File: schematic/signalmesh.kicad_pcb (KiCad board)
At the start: 2 copper layers, 387 x 151 mm, 136 parts, among them J1 FPGA I/O, J10 INA219_CONFIG, J11 INA219_CONFIG, J12 AAM_DBG, J13 DSM_DBG, J14 ACM_DBG, J15 INA219_CONFIG, J16 DSM_DBG, J17 LCD_display, J18 LCD_display, J2 FPGA I/O, J3 LCD_display, J4 TDM_DBG, J5 INA219_CONFIG, J6 INA219_CONFIG, J7 INA219_CONFIG, J8 FPGA I/O, J9 FPGA I/O, U1 NUCLEO-H753ZI, U10 INA219AxD, U11 INA219AxD, U12 INA219AxD, U13 INA219AxD, U14 W25Q128JVS, U15 AP2112K-3.3, U16 74HC4050D, U17 NUCLEO-H753ZI, U18 HDSP-7503, U19 HDSP-7503, U2 HDSP-7503, U20 INA219AxD, U21 74HC4050D, U22 AP2112K-3.3, U23 W25Q128JVS, U24 74HC4050D, U25 AP2112K-3.3, U26 W25Q128JVS, U27 MCP2551-I-P, U28 74LVC1G3157, U29 MCP2551-I-P, U3 NUCLEO-F303RE, U30 MCP2551-I-P, U31 MCP2551-I-P, U4 YAAJ_BluePill_Part_Like, U5 24LC256-I_SN, U6 BME280, U7 INA219AxD, U8 24LC256-I_SN, U9 NUCLEO-F446RE

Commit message: all connections appear valid. some silkscreen clipping
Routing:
- net GND: track 169.3 -> 142.3 mm
- net ACM_SPI_MOSI: track 129.6 -> 107.5 mm
- net /CAN-: track 84.8 -> 64.5 mm, vias 0 -> 2
- net TDM_VDD: track 324.2 -> 314.5 mm, vias 4 -> 5
- net UUM_SPI1_MISO: track 66.4 -> 75.1 mm, vias 1 -> 2
- net Net-(U14-DO/IO_{1}): track 20.6 -> 28.7 mm, vias 0 -> 2
- net 5V_7SDD: track 457.5 -> 465.5 mm
- net AAM_FMC_D10: track 88.8 -> 80.9 mm, vias 1 -> 2
- net Net-(D26-A): track 11.6 -> 3.88 mm
- net TDM_I2C1_SCL: track 360.0 -> 352.6 mm, vias 6 -> 8
- net AAM_FMC_D11: track 79.4 -> 72.4 mm
- net AAM_FMC_D8: track 90.3 -> 83.4 mm
- net DSM_DBG_RX: track 87.4 -> 94.1 mm, vias 0 -> 1
- net DSM_VDD: track 182.4 -> 175.7 mm
- net UUM_SPI1_MISO_B: track 33.3 -> 26.8 mm
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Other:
- copper layers 2 -> 4

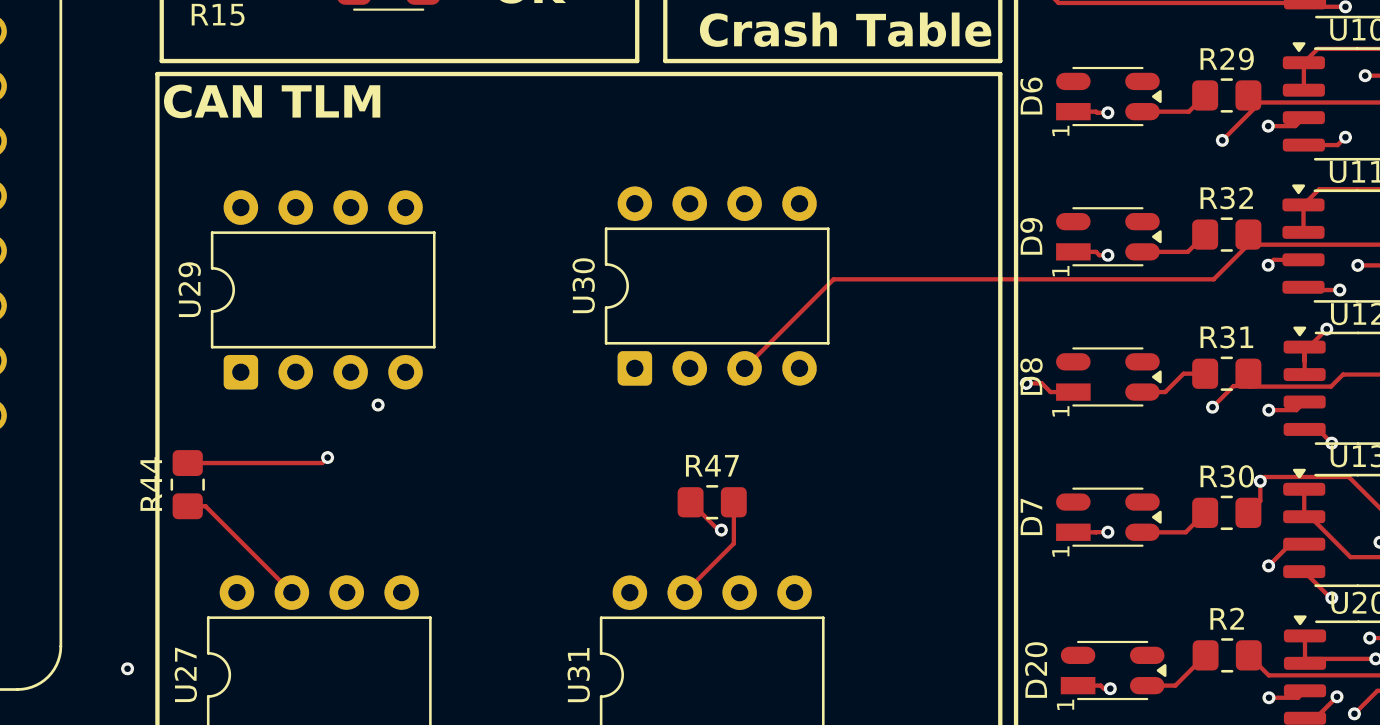
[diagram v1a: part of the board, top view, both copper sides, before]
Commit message: my CAN trscvr LAYOUT sucks
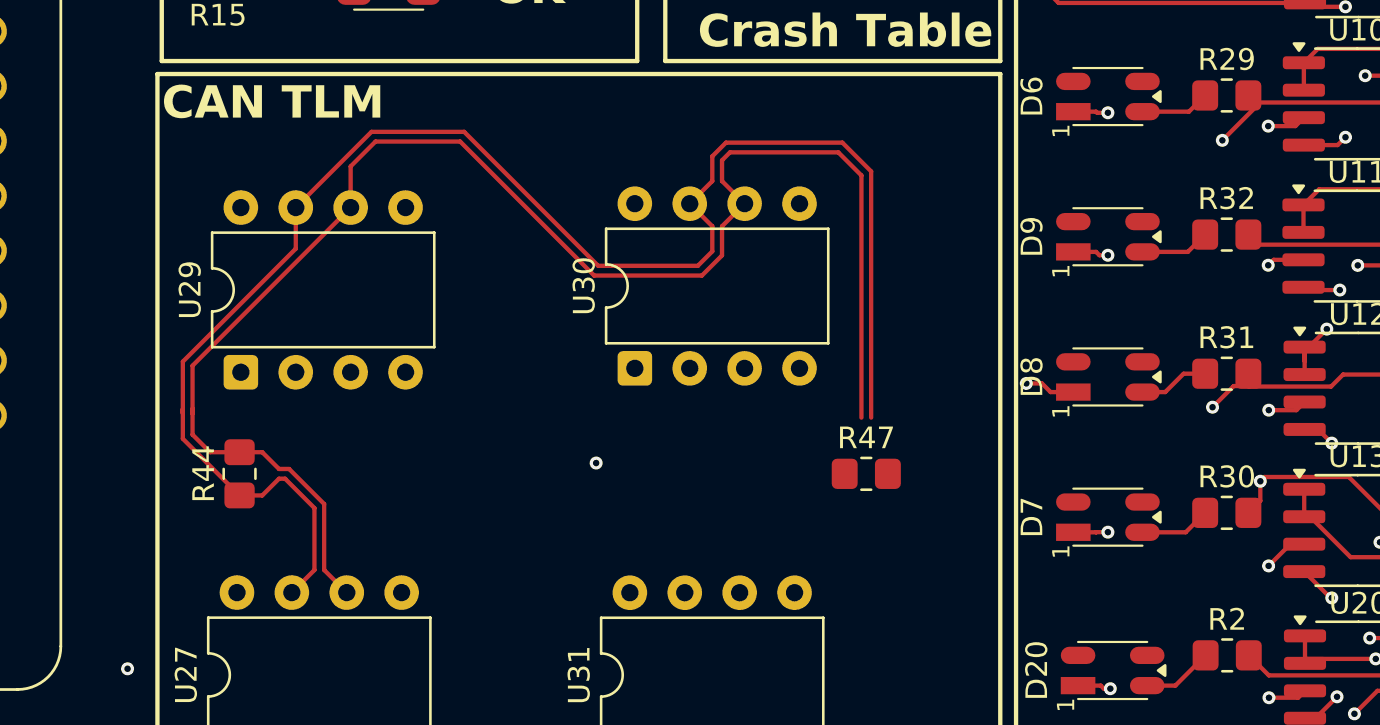
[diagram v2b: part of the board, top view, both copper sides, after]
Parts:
- moved R47 7.25 mm to (520.4, 179.5)
- moved R44 2.45 mm to (491.4, 179.5)
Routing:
- net /CAN-: track 64.5 -> 71.9 mm, vias 2 -> 0
- net /CAN+: track 68.1 -> 74.1 mm
- net VDD_UUM: track 453.8 -> 451.7 mm

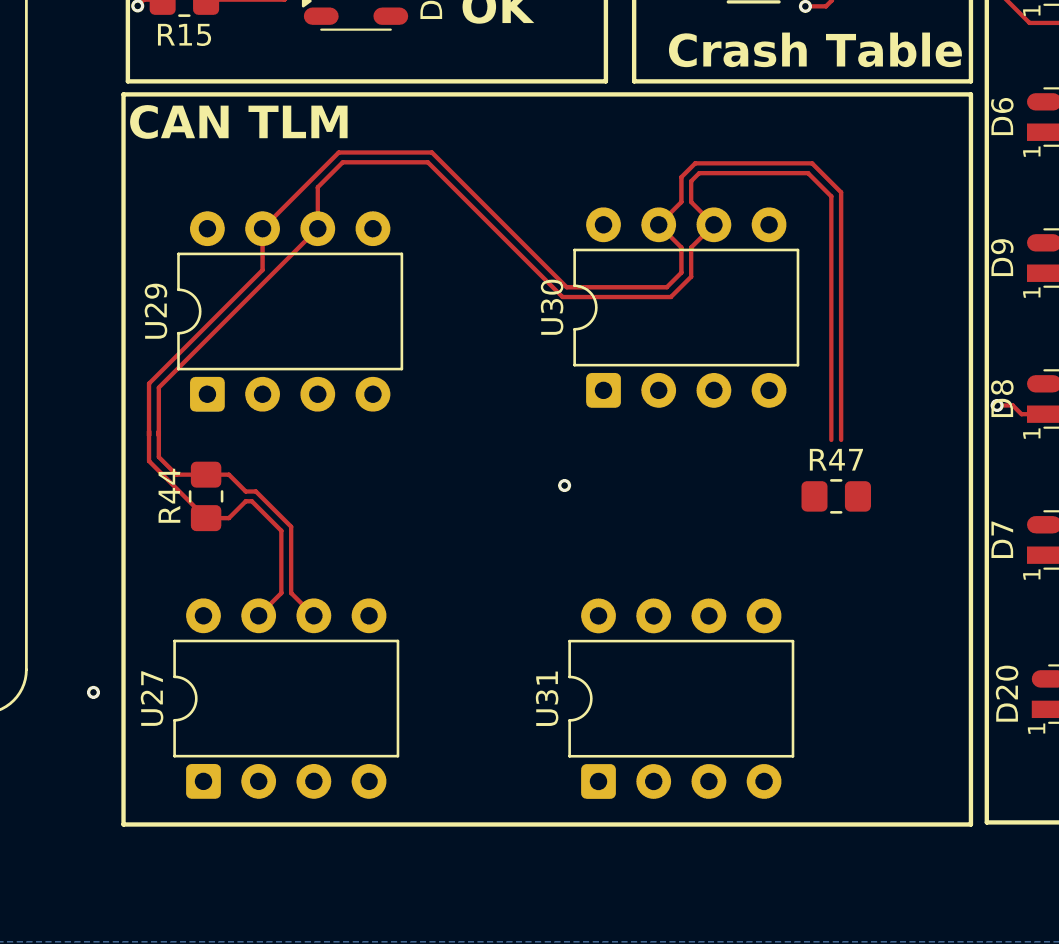
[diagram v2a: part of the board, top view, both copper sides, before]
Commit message: CAN pos neg lines routed. broke other shit. autoroute hates me
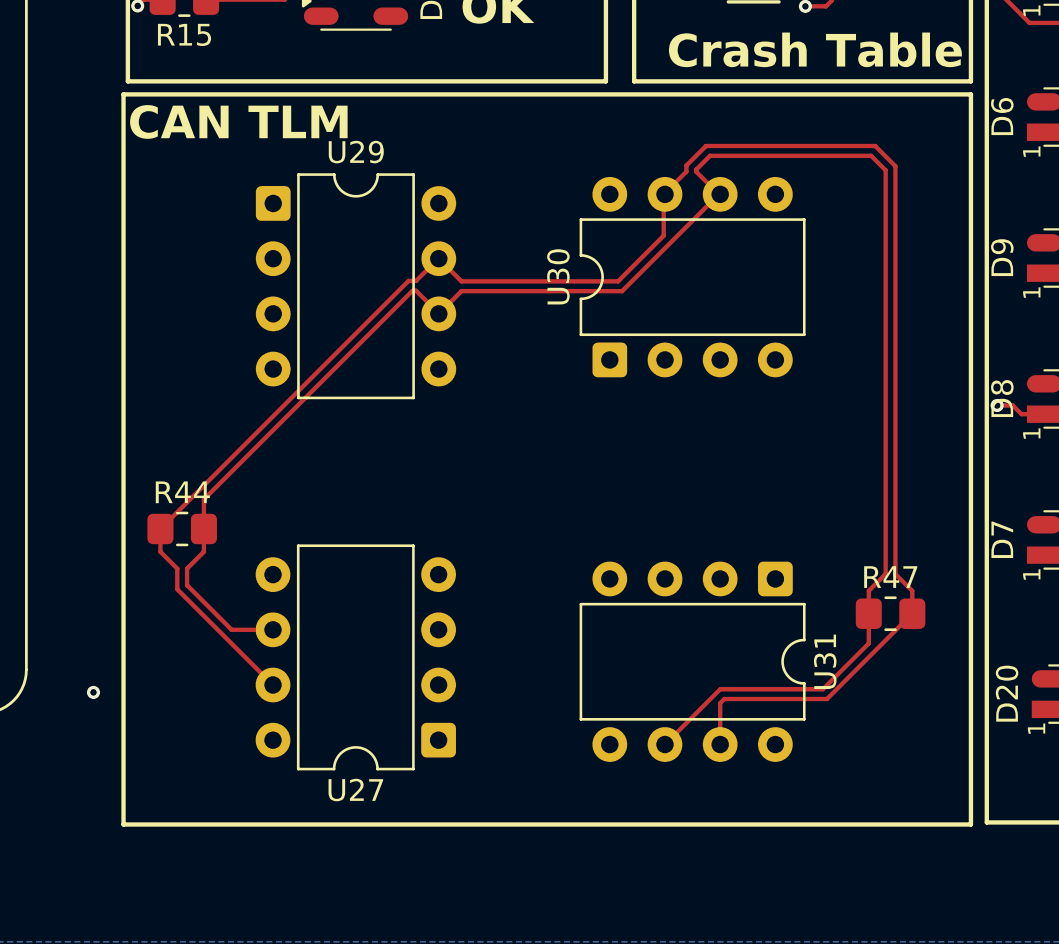
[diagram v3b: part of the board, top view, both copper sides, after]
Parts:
- moved U31 12.4 mm to (517.6, 183.3), turned to -90 degrees
- moved U27 11.0 mm to (502.1, 190.7), turned to 180 degrees
- moved U29 9.29 mm to (494.5, 166.0), turned to 0 degrees
- moved R47 5.95 mm to (522.9, 184.9)
- moved R44 1.86 mm to (490.3, 181.0), turned to 0 degrees
- moved U30 1.43 mm to (510.0, 173.2)
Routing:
- net /CAN+: track 74.1 -> 86.4 mm
- net /CAN-: track 71.9 -> 83.7 mm
- net VDD_UUM: vias 5 -> 4

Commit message: routed no errors
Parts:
- moved J18 220.2 mm to (391.3, 196.2), turned to -90 degrees
- moved J17 70.8 mm to (377.3, 196.2)
- moved J3 49.0 mm to (367.4, 196.2)
- moved C7 33.2 mm to (548.7, 157.8), turned to 180 degrees
- moved C1 33.2 mm to (548.7, 191.0), turned to 180 degrees
- moved C2 20.2 mm to (548.7, 184.5), turned to 180 degrees
- moved C5 19.8 mm to (548.7, 164.5), turned to 180 degrees
- moved C3 7.21 mm to (548.7, 178.0), turned to 180 degrees
- moved C4 6.29 mm to (548.7, 171.3), turned to 180 degrees
- moved J15 1.90 mm to (556.8, 188.0)
- moved D7 0.52 mm to (531.8, 182.0)
- moved D8 0.40 mm to (531.8, 175.4)
- moved R2 0.32 mm to (537.0, 188.2)
- moved R30 0.31 mm to (537.0, 181.6)
- moved R26 0.31 mm to (552.6, 180.5)
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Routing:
- net TDM_VDD: track 314.5 -> 239.3 mm, vias 5 -> 4
- net DSM_VDD: track 175.7 -> 137.8 mm, vias 2 -> 1
- net AAM_VDD: track 159.8 -> 135.5 mm
- net VDD_UUM: track 451.7 -> 432.0 mm, vias 4 -> 5
- net TDM_I2C1_SCL: track 352.6 -> 333.0 mm, vias 8 -> 10
- net UUM_CAN_TD: track 275.6 -> 291.4 mm
- net TDM_I2C1_SDA: track 353.9 -> 341.5 mm, vias 10 -> 5
- net DSM_DBG_TX: track 85.6 -> 97.5 mm, vias 0 -> 1
- net TDM_DBG_TX: track 209.2 -> 220.2 mm
- net 5V_UUM: track 302.6 -> 313.5 mm
- net VDD_AAM: track 54.3 -> 65.1 mm, vias 1 -> 2
- net UUM_SPI1_MISO: track 75.1 -> 64.5 mm, vias 2 -> 1
- net ACM_SPI_MOSI: track 107.5 -> 117.8 mm, vias 1 -> 2
- net ACM_SPI_SCLK: track 106.4 -> 115.5 mm
- net AAM_FMC_NL: track 126.6 -> 118.4 mm, vias 1 -> 2
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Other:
- board text added: "AAM DSPLY"
- board text added: "SCL"
- board text added: "SDA"
- board text added: "VDD"

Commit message: progress. might have enough of the vital stuff routed to get the autorouter working for the rest. not sure if it will follow rules though
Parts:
- added J19: AudioJack3, Connector_Audio:Jack_3.5mm_CUI_SJ-3523-SMT_Horizontal, F.Cu at (267.1, 61.0)
- C1, C10, C2, C3, C4, C5, C6, C7, C8, C9: footprint Capacitor_SMD:C_0201_0603Metric -> Capacitor_SMD:C_0805_2012Metric
- D1, D10, D13, D14, D15, D16, D17, D18, D19, D2, D20, D21, D22, D23, D24, D25, D26, D27, D3, D4, D5, D6, D7, D8, D9: footprint LED_SMD:LED_Kingbright_KPBD-3224 -> LED_SMD:LED_0603_1608Metric
- J17, J18, J3: footprint Connector_PinHeader_1.00mm:PinHeader_1x04_P1.00mm_Horizontal -> Connector_PinHeader_1.00mm:PinHeader_1x04_P1.00mm_Vertical_SMD_Pin1Left
- moved U6 2.96 mm to (381.8, 187.0)
- moved J3 1.94 mm to (365.9, 197.4)
- moved J18 1.93 mm to (389.8, 197.4)
- moved U31 1.79 mm to (516.8, 181.7)
- moved U29 1.79 mm to (493.7, 164.4)
- moved R44 1.79 mm to (489.5, 179.4)
- moved U27 1.79 mm to (501.3, 189.1)
- moved U30 1.79 mm to (509.2, 171.6)
- moved R47 1.79 mm to (522.1, 183.3)
- moved J17 1.40 mm to (378.0, 197.4)
- moved R2 1.40 mm to (535.6, 188.2)
- moved R27 1.40 mm to (535.6, 155.6)
- moved R29 1.40 mm to (535.6, 162.0)
- moved R30 1.40 mm to (535.6, 181.6)
- moved R31 1.40 mm to (535.6, 174.9)
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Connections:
- R1 pad 2: 7SDD_VDD -> 5V_7SDD
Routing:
- net 5V_7SDD: track 459.2 -> 0.00 mm, vias 2 -> 0
- net VDD_UUM: track 432.0 -> 11.2 mm, vias 5 -> 0
- net 5V_AAM: track 326.9 -> 0.00 mm, vias 2 -> 0
- net 5V_UUM: track 313.5 -> 0.00 mm, vias 2 -> 0
- net UUM_CAN_TD: track 291.4 -> 0.00 mm, vias 1 -> 0
- net UUM_CAN_RD: track 278.7 -> 0.00 mm, vias 1 -> 0
- net TDM_I2C1_SDA: track 341.5 -> 167.6 mm, vias 5 -> 9
- net AAM_FMC_D2: track 170.2 -> 9.00 mm, vias 1 -> 0
- net AAM_FMC_D3: track 161.9 -> 9.00 mm, vias 1 -> 0
- net 5V_ACM: track 159.8 -> 9.00 mm, vias 1 -> 0
- net AAM_INTRPT_RX: track 148.6 -> 0.00 mm, vias 1 -> 0
- net AAM_INTRPT_TX: track 147.8 -> 0.00 mm, vias 1 -> 0
- net DSM_VDD: track 137.8 -> 0.00 mm, vias 1 -> 0
- net ACM_FMC_D14: track 146.6 -> 9.00 mm, vias 1 -> 0
- net VDD_ACM: track 158.6 -> 22.5 mm, vias 2 -> 0
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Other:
- board text removed: "100nF"
